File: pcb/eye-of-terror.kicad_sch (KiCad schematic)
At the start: 226 parts, among them J1 Conn_01x02_Socket, J2 G-Switch GT-USB-7055E, J3 Conn_01x04, J4 Conn_01x04, J5 Conn_01x03, J6 Conn_01x02_Socket, J7 Conn_01x02_Socket, J8 Conn_01x03, Q1 IPT020N10N3, Q10 ALS-PT19-315C/L177/TR8, Q11 ALS-PT19-315C/L177/TR8, Q12 ALS-PT19-315C/L177/TR8, Q13 ALS-PT19-315C/L177/TR8, Q14 ALS-PT19-315C/L177/TR8, Q15 ALS-PT19-315C/L177/TR8, Q16 ALS-PT19-315C/L177/TR8, Q17 ALS-PT19-315C/L177/TR8, Q2 IPT020N10N3, Q3 IPT020N10N3, Q4 IPT020N10N3, Q5 IPT020N10N3, Q6 IPT020N10N3, Q7 ALS-PT19-315C/L177/TR8, Q8 ALS-PT19-315C/L177/TR8, Q9 ALS-PT19-315C/L177/TR8, SW1 SW_Push, SW2 SW_Push, U1 RP2350B, U2 TD1660, U3 AP63205WU-7, U4 LSM6DS3, U5 W25Q32JVSS, U7 DRV8353HRTAR, Y1 ABM8-272-T3

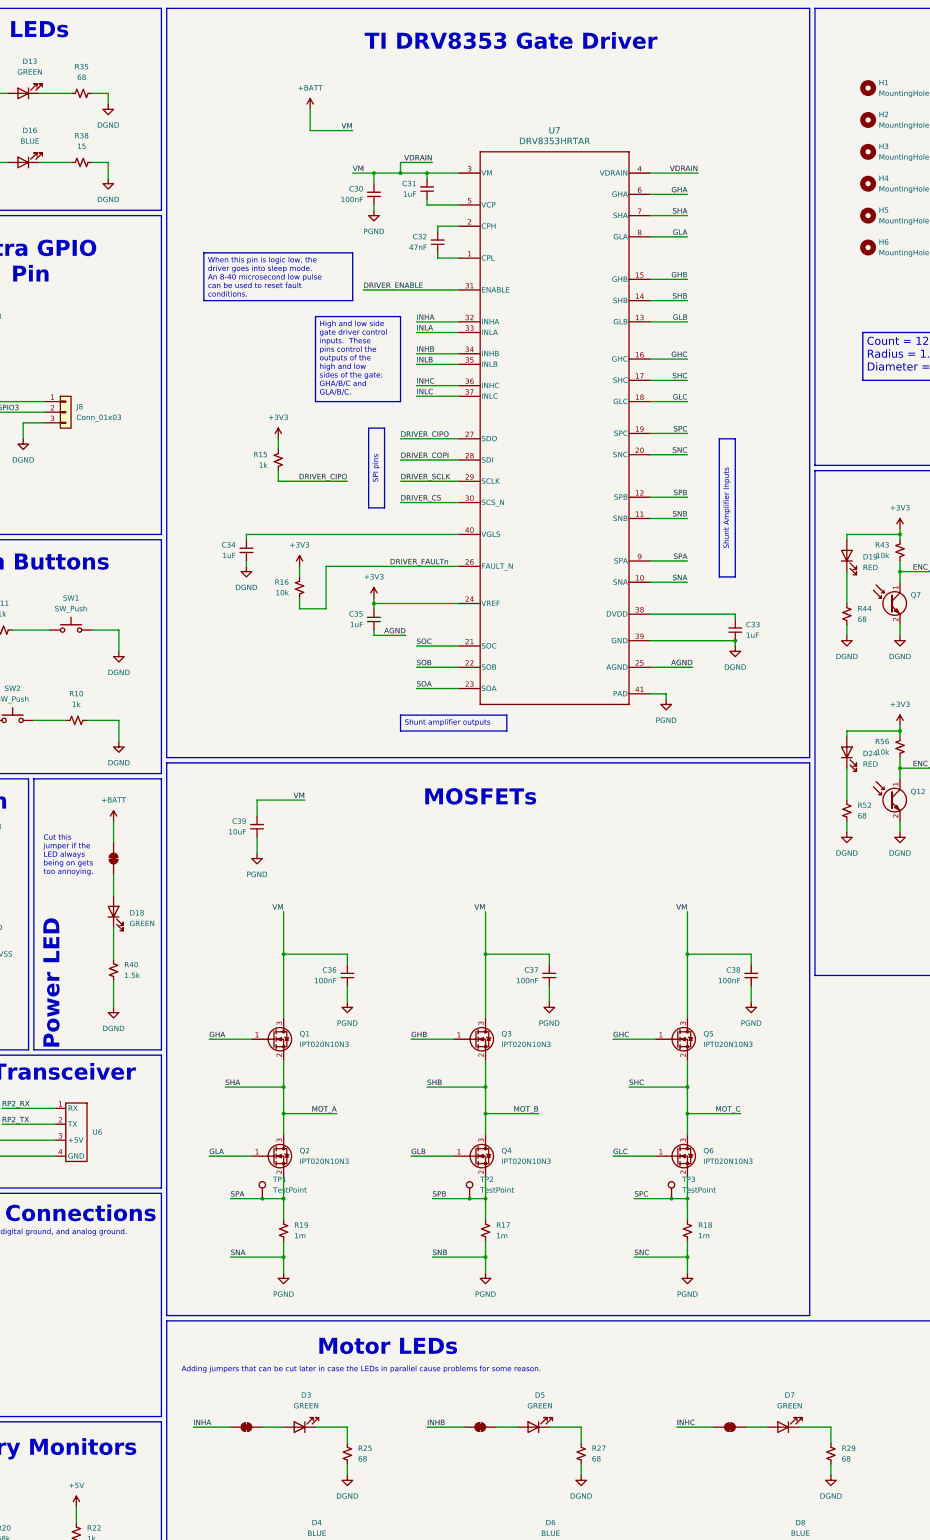
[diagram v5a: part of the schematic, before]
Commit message: added placement dxf for encoders to layout
i think it lines up alright like this
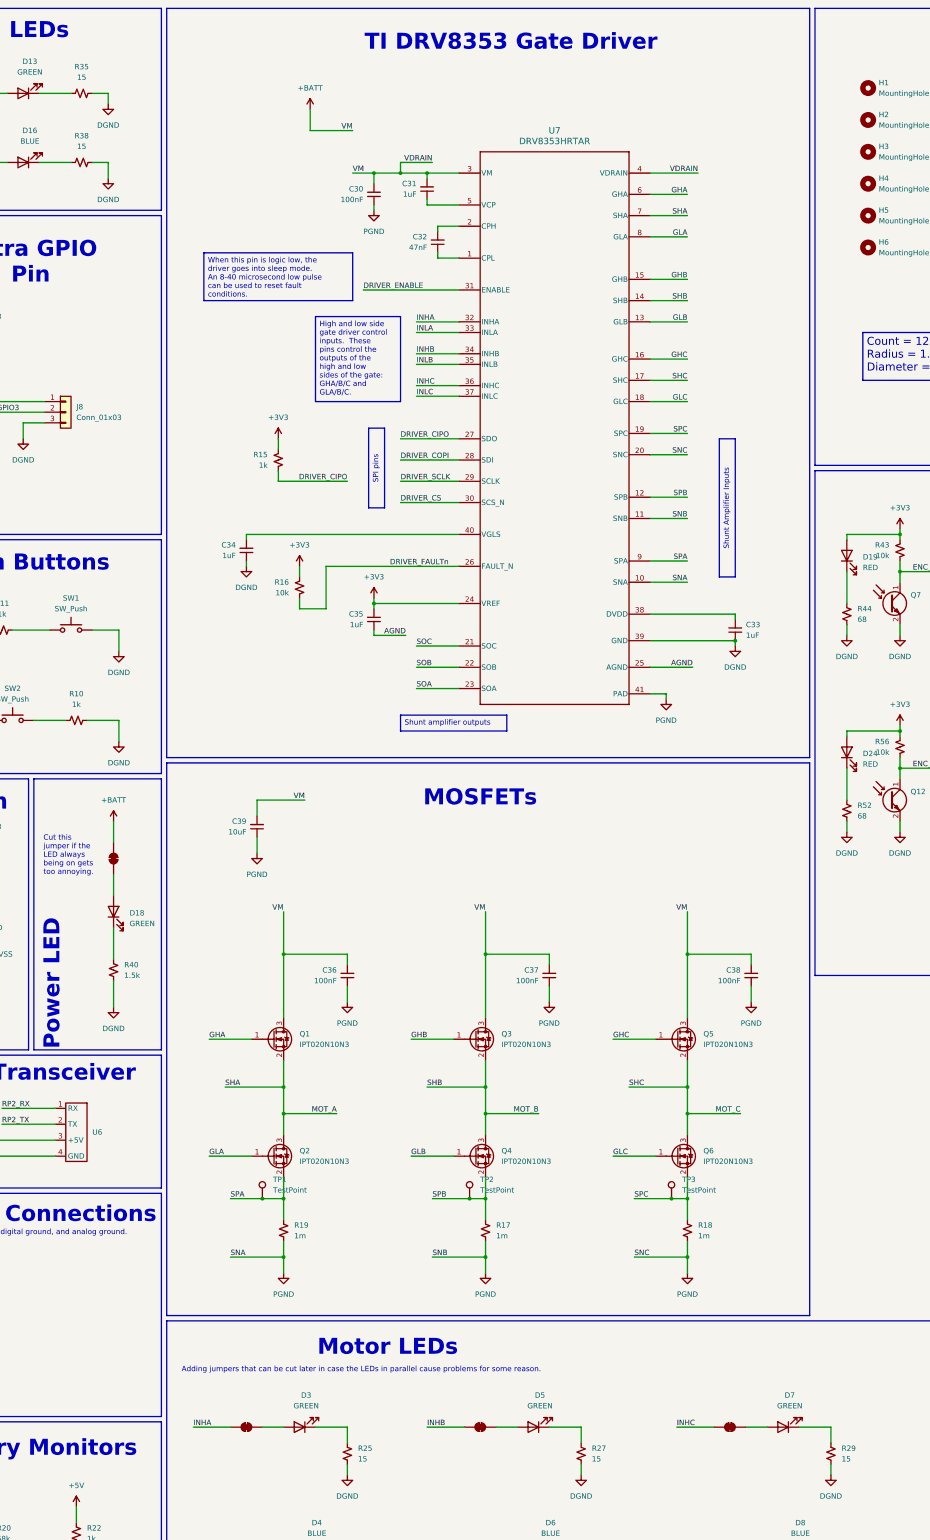
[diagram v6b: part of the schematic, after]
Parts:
- R25, R27, R29, R35: value 68 -> 15; footprint Resistor_SMD:R_0402_1005Metric -> Resistor_SMD:R_0603_1608Metric
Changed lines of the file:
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@@
 			)
 		)
-		(property "Value" "68"
+		(property "Value" "15"
 			(at 280.67 359.4099 0)
 			(effects
@@
 			)
 		)
-		(property "Footprint" "Resistor_SMD:R_0402_1005Metric"
+		(property "Footprint" "Resistor_SMD:R_0603_1608Metric"
 			(at 278.13 358.14 0)
 			(effects
@@
 			)
 		)
-		(property "Value" "68"
+		(property "Value" "15"
 			(at 336.55 359.4099 0)
 			(effects
@@
 			)
 		)
-		(property "Footprint" "Resistor_SMD:R_0402_1005Metric"
+		(property "Footprint" "Resistor_SMD:R_0603_1608Metric"
 			(at 334.01 358.14 0)
 			(effects
@@
 			)
 		)
-		(property "Value" "68"
+		(property "Value" "15"
 			(at 396.24 359.4099 0)
 			(effects
@@
 			)
 		)
-		(property "Footprint" "Resistor_SMD:R_0402_1005Metric"
+		(property "Footprint" "Resistor_SMD:R_0603_1608Metric"
 			(at 393.7 358.14 0)
 			(effects
@@
 			)
 		)
-		(property "Value" "68"
+		(property "Value" "15"
 			(at 214.63 29.21 90)
 			(effects
@@
 			)
 		)
-		(property "Footprint" "Resistor_SMD:R_0402_1005Metric"
+		(property "Footprint" "Resistor_SMD:R_0603_1608Metric"
 			(at 214.63 33.02 0)
 			(effects

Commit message: deleted 11th encoder pin (we only use 10)
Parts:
- removed D29: RED, Diode_SMD:D_1206_3216Metric, symbol Device:LED
- removed Q17: ALS-PT19-315C/L177/TR8, LED_SMD:LED_0603_1608Metric, symbol Device:Q_Photo_NPN
- removed R61: 68, Resistor_SMD:R_0402_1005Metric, symbol Device:R_Small_US
- removed R65: 10k, Resistor_SMD:R_0402_1005Metric, symbol Device:R_Small_US
- U6: value ~ -> (none)
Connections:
- net ENC_SENSE_11: no longer names the net of U1.47 (GPIO38)
- no-connect marks 8 -> 9

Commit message: WIP version 2
* (tried to) remove backup files from repo
* increased current-limiting resistors on green and blue LEDs
* added pins for motor windings
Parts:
- removed R20: 68k, Resistor_SMD:R_0603_1608Metric, symbol Device:R_Small_US
- removed R21: 10k, Resistor_SMD:R_0402_1005Metric, symbol Device:R_Small_US
- removed R22: 1k, Resistor_SMD:R_0402_1005Metric, symbol Device:R_Small_US
- removed R23: 1.5k, Resistor_SMD:R_1210_3225Metric, symbol Device:R_Small_US
- added NT1, NT2: NetTie_2, NetTie:NetTie-2_SMD_Pad2.0mm, symbol Device:NetTie_2
- added TP4, TP5: PHASE_U, symbol Connector:TestPoint
- added TP6, TP7: PHASE_V, symbol Connector:TestPoint
- added TP8, TP9: PHASE_W, symbol Connector:TestPoint
- D18: value GREEN -> RED
- R25, R26, R27, R28, R29, R30, R35, R38: value 15 -> 100
- R40: value 1.5k -> 1k
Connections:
- net DGND: now also NT1.2, NT2.2
- net MOT_A: now also TP4.1, TP7.1
- net MOT_B: now also TP5.1, TP9.1
- net MOT_C: now also TP6.1, TP8.1
- net PGND: now also NT1.1, NT2.1; no longer U7.41 (PAD)
- no-connect marks 9 -> 10
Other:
- note added: "Motor Winding Connections"
- note added: "Phases U, V, and W connect to outputs A, B, and C in a delta configuration."
